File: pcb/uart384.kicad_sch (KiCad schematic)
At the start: 32 parts, among them IC1 ICE40LP384-SG32, J1 USB_A, J2 TC2050, J3 Conn_02x06_Odd_Even, SW1 SW_Push, U1 CP2102-QFN28, U2 AT25DF256-XMHN-T, U3 MIC5365-1.2YC5, Y1 XO32

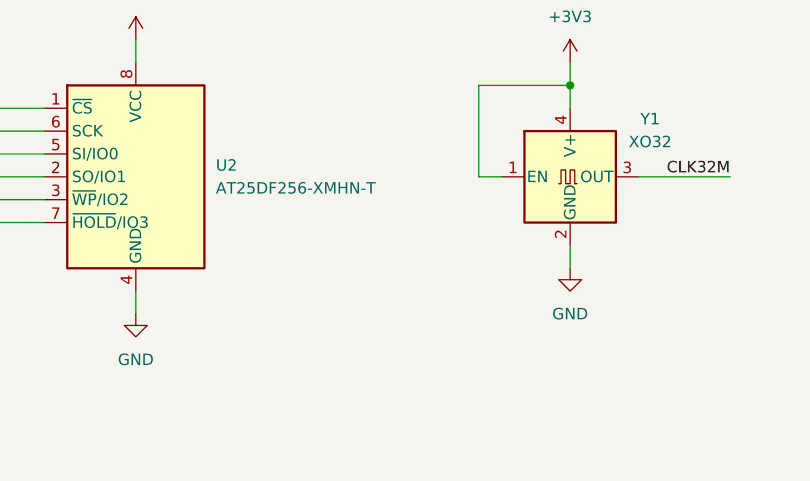
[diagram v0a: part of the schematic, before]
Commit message: PCBv1 Errata: Mismatch between SPI flash footprint and selected part#.
Part now must be SOIC-8 150mil / SOP-8 150mil.
Updated part#s in schematic / PCB.
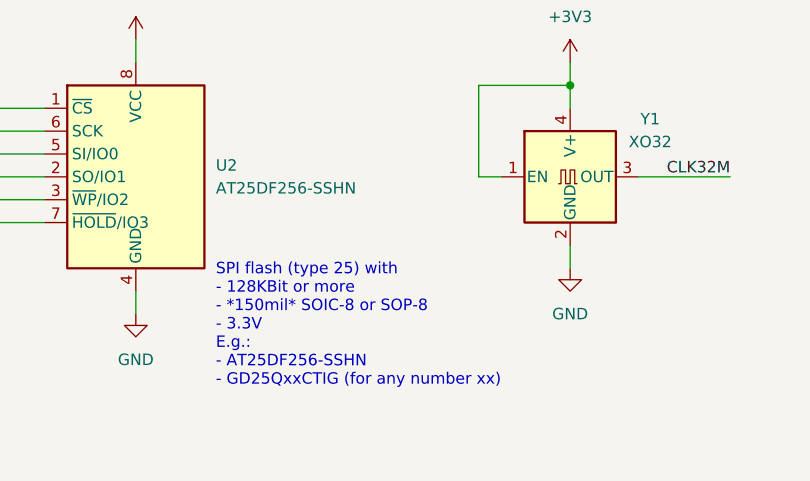
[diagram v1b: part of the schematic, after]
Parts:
- U2: value AT25DF256-XMHN-T -> AT25DF256-SSHN
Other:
- note added: "SPI flash (type 25) with - 128KBit or more - *150mil* SOIC-8 or SOP-8 - 3.3V E.g.: - AT25DF256-SSHN - GD25QxxCTIG (for any number xx)"
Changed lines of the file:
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@@
 	(title_block
 		(title "UART384")
-		(date "2025-08-26")
-		(rev "v1.0")
+		(rev "v1.1~dev")
 		(comment 1 "a USB/UART enabled dev-board for the ice40LP384")
 		(comment 2 "https://github.com/dpiegdon/uart384")
 	)
+	(text "SPI flash (type 25) with\n- 128KBit or more\n- *150mil* SOIC-8 or SOP-8\n- 3.3V\nE.g.:\n- AT25DF256-SSHN\n- GD25QxxCTIG (for any number xx)\n"
+		(exclude_from_sim no)
+		(at 114.3 179.07 0)
+		(effects
+			(font
+				(size 1.27 1.27)
+			)
+			(justify left)
+		)
+	)
 	(text "Close to VCCIO pins"
 		(exclude_from_sim no)
@@
 			)
 		)
-		(property "Value" "AT25DF256-XMHN-T"
+		(property "Value" "AT25DF256-SSHN"
 			(at 114.3 163.8299 0)
 			(effects
@@
 			)
 		)
-		(property "Description" "8-Mbit, 2.5V Minimum SPI Serial Flash Memory with Dual-I/O and Quad-I/O Support, SOIC-8"
+		(property "Description" "Any 3.3V SPI flash with >= 128KBit, SOIC-8 150mil or SOP-8 150mil"
 			(at 105.41 162.56 0)
 			(effects

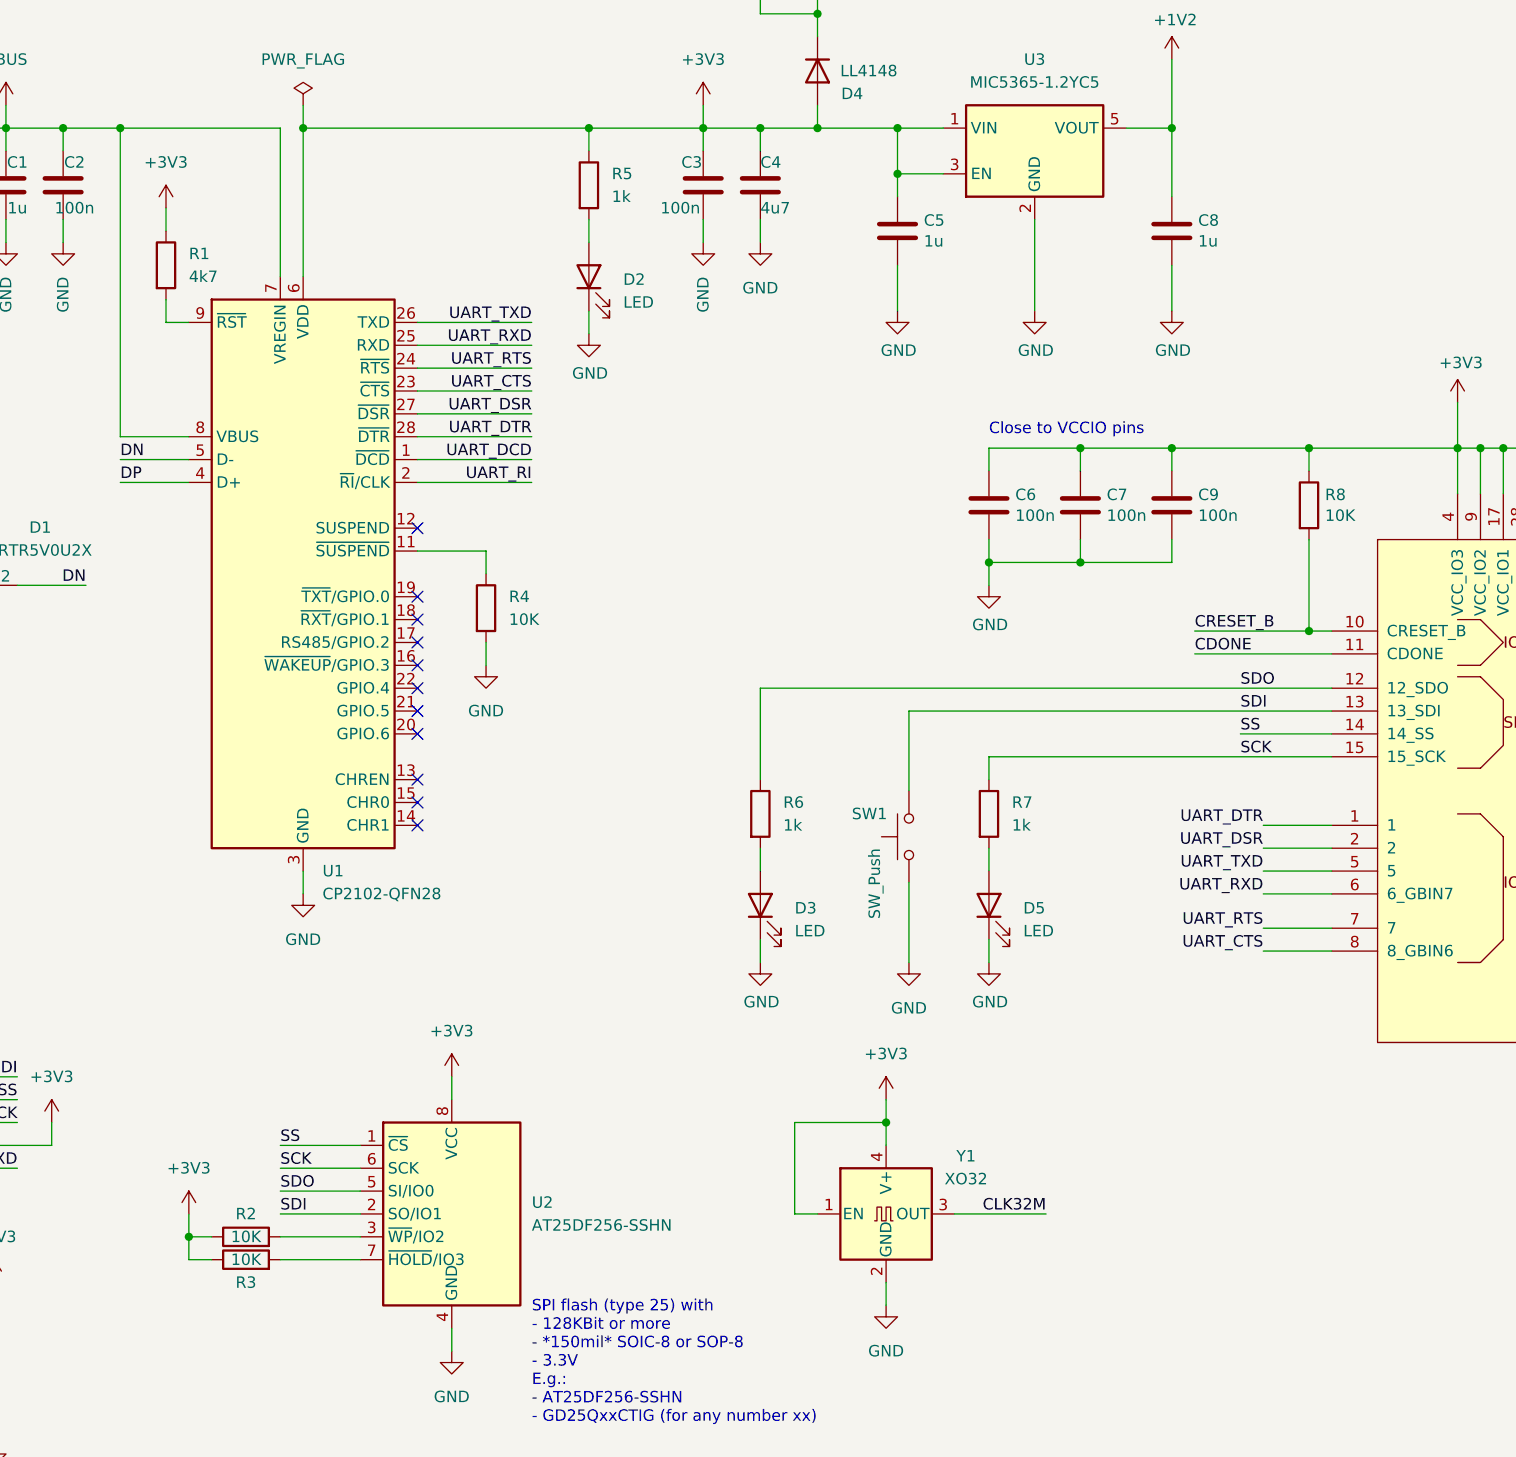
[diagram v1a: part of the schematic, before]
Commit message: PCBv1 Errata: SPI SS pullup missing
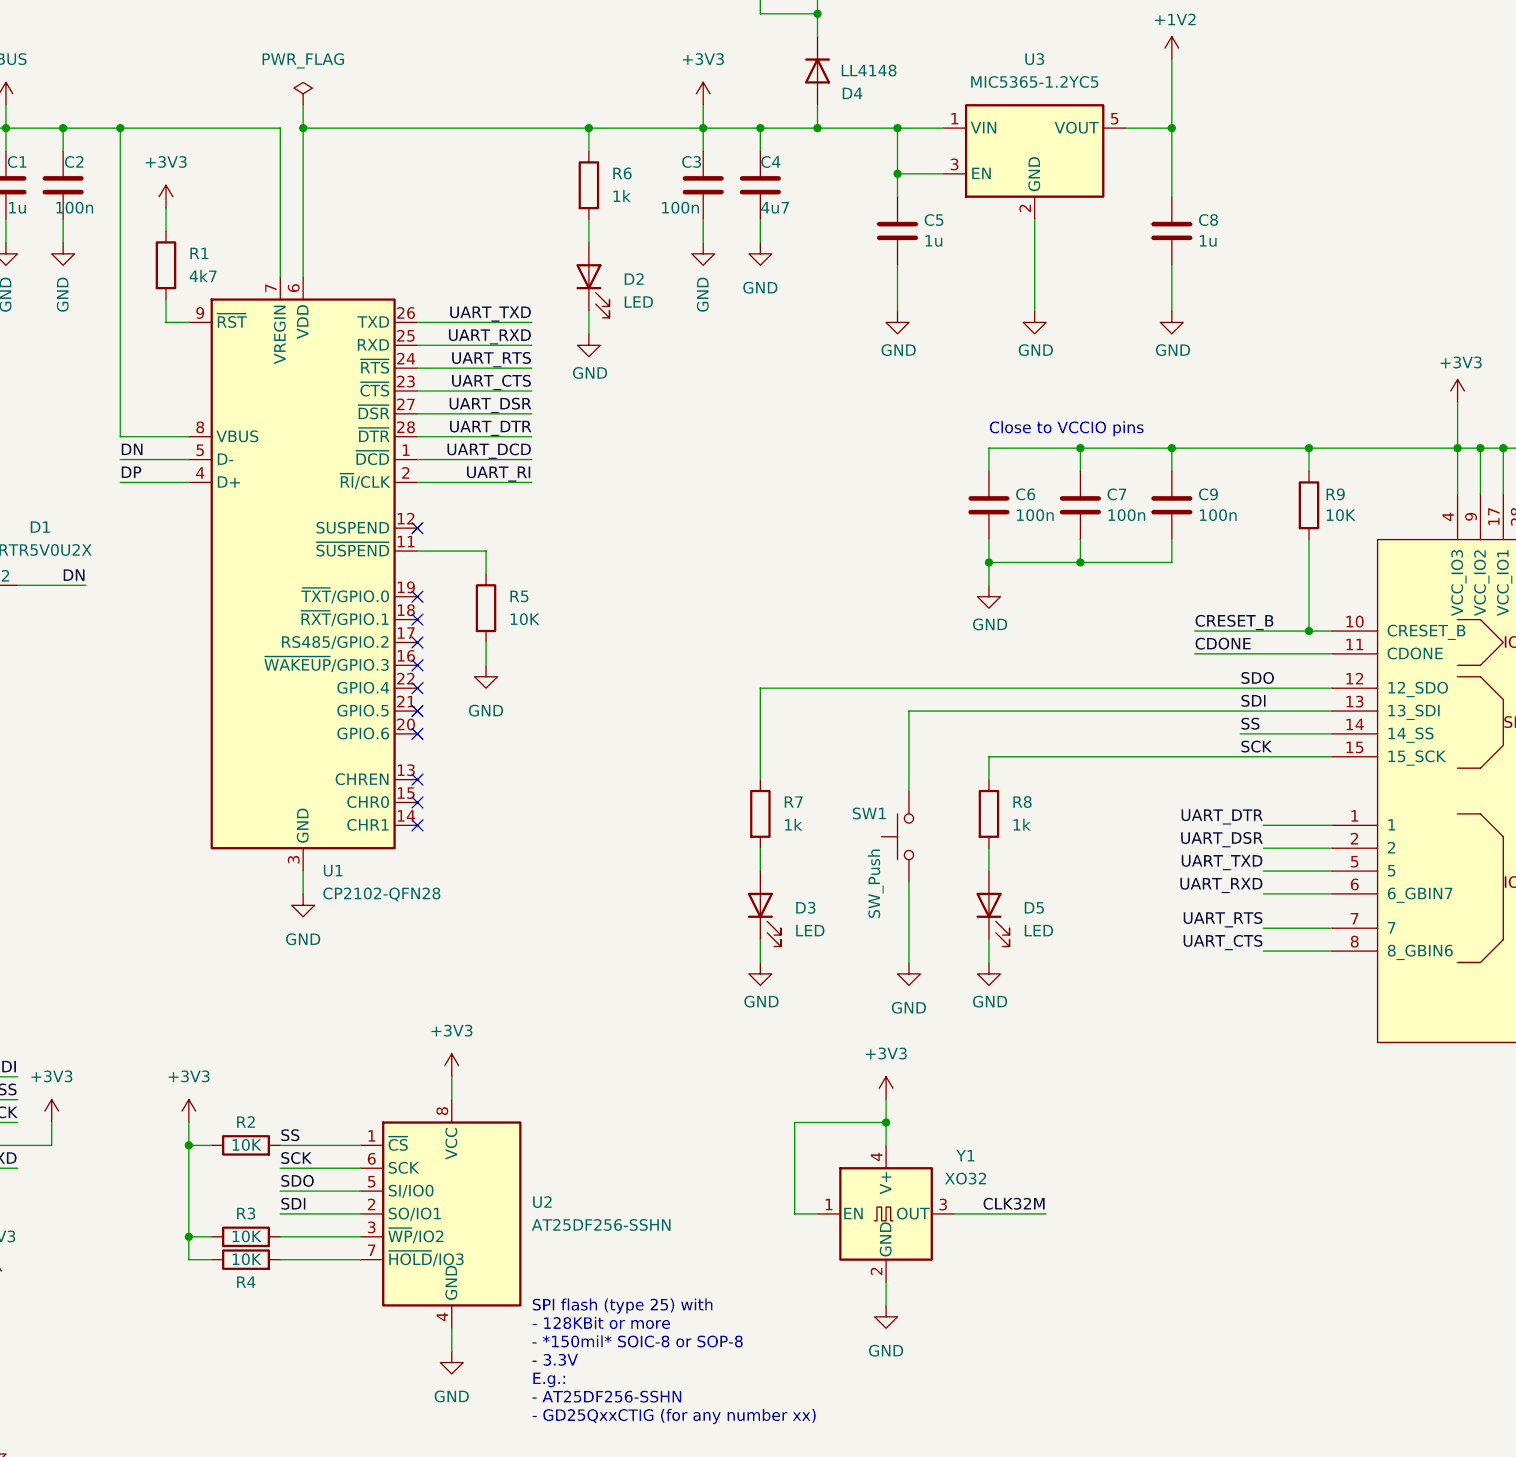
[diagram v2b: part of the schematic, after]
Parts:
- added R2: 10K, Resistor_SMD:R_0603_1608Metric, symbol Device:R
- renumbered R2 to R3, R3 to R4, R4 to R5, R5 to R6, R6 to R7, R7 to R8, R8 to R9
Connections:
- net +3V3: now also R2.1
- net SS: now also R2.2
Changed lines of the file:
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@@
 	)
 	(junction
+		(at 76.2 154.94)
+		(diameter 0)
+		(color 0 0 0 0)
+	)
+	(junction
 		(at 175.26 90.17)
 		(diameter 0)
@@
 	(wire
 		(pts
+			(xy 76.2 154.94) (xy 76.2 165.1)
+		)
+		(stroke
+			(width 0)
+			(type default)
+		)
+	)
+	(wire
+		(pts
 			(xy 139.7 29.21) (xy 146.05 29.21)
 		)
@@
 	(wire
 		(pts
+			(xy 76.2 154.94) (xy 78.74 154.94)
+		)
+		(stroke
+			(width 0)
+			(type default)
+		)
+	)
+	(wire
+		(pts
 			(xy 68.58 41.91) (xy 62.23 41.91)
 		)
@@
 	(wire
 		(pts
-			(xy 76.2 162.56) (xy 76.2 165.1)
+			(xy 76.2 152.4) (xy 76.2 154.94)
 		)
 		(stroke
@@
 		(dnp no)
 		(fields_autoplaced yes)
-		(property "Reference" "R7"
+		(property "Reference" "R8"
 			(at 167.64 116.8399 0)
 			(effects
@@
 			(project ""
 				(path "/951aeac3-6c61-42a5-aa61-f58713889333"
-					(reference "R7")
+					(reference "R8")
 					(unit 1)
 				)
@@
 		(dnp no)
 		(fields_autoplaced yes)
-		(property "Reference" "R4"
+		(property "Reference" "R5"
 			(at 111.76 93.9799 0)
 			(effects
@@
 			(project ""
 				(path "/951aeac3-6c61-42a5-aa61-f58713889333"
-					(reference "R4")
+					(reference "R5")
 					(unit 1)
 				)
@@
 	(symbol
 		(lib_id "power:+3V3")
-		(at 76.2 162.56 0)
+		(at 76.2 152.4 0)
 		(unit 1)
 		(exclude_from_sim no)
@@
 		(fields_autoplaced yes)
 		(property "Reference" "#PWR014"
-			(at 76.2 166.37 0)
+			(at 76.2 156.21 0)
 			(effects
 				(font
@@
 		)
 		(property "Value" "+3V3"
-			(at 76.2 157.48 0)
+			(at 76.2 147.32 0)
 			(effects
 				(font
@@
 		)
 		(property "Footprint" ""
-			(at 76.2 162.56 0)
+			(at 76.2 152.4 0)
 			(effects
 				(font
@@
 		)
 		(property "Datasheet" ""
-			(at 76.2 162.56 0)
+			(at 76.2 152.4 0)
 			(effects
 				(font
@@
 		)
 		(property "Description" "Power symbol creates a global label with name \"+3V3\""
-			(at 76.2 162.56 0)
+			(at 76.2 152.4 0)
 			(effects
 				(font
@@
 		(on_board yes)
 		(dnp no)
-		(property "Reference" "R3"
+		(property "Reference" "R4"
 			(at 82.55 170.18 90)
 			(effects
@@
 			(project ""
 				(path "/951aeac3-6c61-42a5-aa61-f58713889333"
-					(reference "R3")
+					(reference "R4")
 					(unit 1)
 				)
@@
 		(on_board yes)
 		(dnp no)
-		(property "Reference" "R2"
+		(property "Reference" "R3"
 			(at 82.55 162.56 90)
 			(effects
@@
 			(project ""
 				(path "/951aeac3-6c61-42a5-aa61-f58713889333"
-					(reference "R2")
+					(reference "R3")
 					(unit 1)
 				)
@@
 		(on_board yes)
 		(dnp no)
-		(property "Reference" "R8"
+		(property "Reference" "R9"
 			(at 202.438 82.6516 0)
 			(effects
@@
 			(project "uart384"
 				(path "/951aeac3-6c61-42a5-aa61-f58713889333"
-					(reference "R8")
+					(reference "R9")
 					(unit 1)
 				)
@@
 		(dnp no)
 		(fields_autoplaced yes)
-		(property "Reference" "R6"
+		(property "Reference" "R7"
 			(at 142.24 116.8399 0)
 			(effects
@@
 			(project "uart384"
 				(path "/951aeac3-6c61-42a5-aa61-f58713889333"
-					(reference "R6")
+					(reference "R7")
 					(unit 1)
 				)
@@
 	)
 	(symbol
+		(lib_id "Device:R")
+		(at 82.55 154.94 90)
+		(unit 1)
+		(exclude_from_sim no)
+		(in_bom yes)
+		(on_board yes)
+		(dnp no)
+		(property "Reference" "R2"
+			(at 82.55 152.4 90)
+			(effects
+				(font
+					(size 1.27 1.27)
+				)
+			)
+		)
+		(property "Value" "10K"
+			(at 82.55 154.94 90)
+			(effects
+				(font
+					(size 1.27 1.27)
+				)
+			)
+		)
+		(property "Footprint" "Resistor_SMD:R_0603_1608Metric"
+			(at 82.55 156.718 90)
+			(effects
+				(font
+					(size 1.27 1.27)
+				)
+				(hide yes)
+			)
+		)
+		(property "Datasheet" "~"
+			(at 82.55 154.94 0)
+			(effects
+				(font
+					(size 1.27 1.27)
+				)
+				(hide yes)
+			)
+		)
+		(property "Description" "Resistor"
+			(at 82.55 154.94 0)
+			(effects
+				(font
+					(size 1.27 1.27)
+				)
+				(hide yes)
+			)
+		)
+		(pin "2"
+		)
+		(pin "1"
+		)
+		(instances
+			(project "uart384"
+				(path "/951aeac3-6c61-42a5-aa61-f58713889333"
+					(reference "R2")
+					(unit 1)
+				)
+			)
+		)
+	)
+	(symbol
 		(lib_id "Device:C")
 		(at 139.7 48.26 0)
@@
 		(dnp no)
 		(fields_autoplaced yes)
-		(property "Reference" "R5"
+		(property "Reference" "R6"
 			(at 123.19 46.9899 0)
 			(effects
@@
 			(project "uart384"
 				(path "/951aeac3-6c61-42a5-aa61-f58713889333"
-					(reference "R5")
+					(reference "R6")
 					(unit 1)
 				)

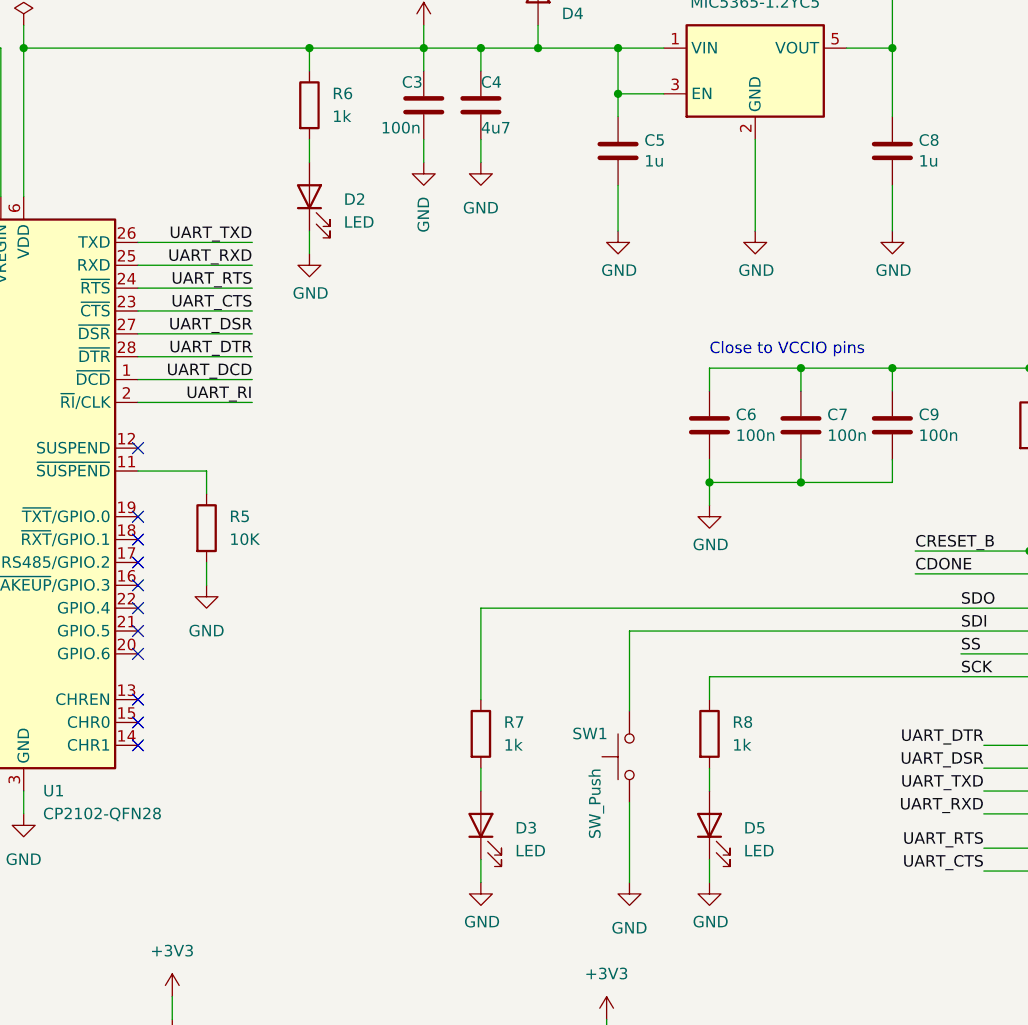
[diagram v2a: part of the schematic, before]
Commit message: name LEDs with used colors. use LEDs for more things.
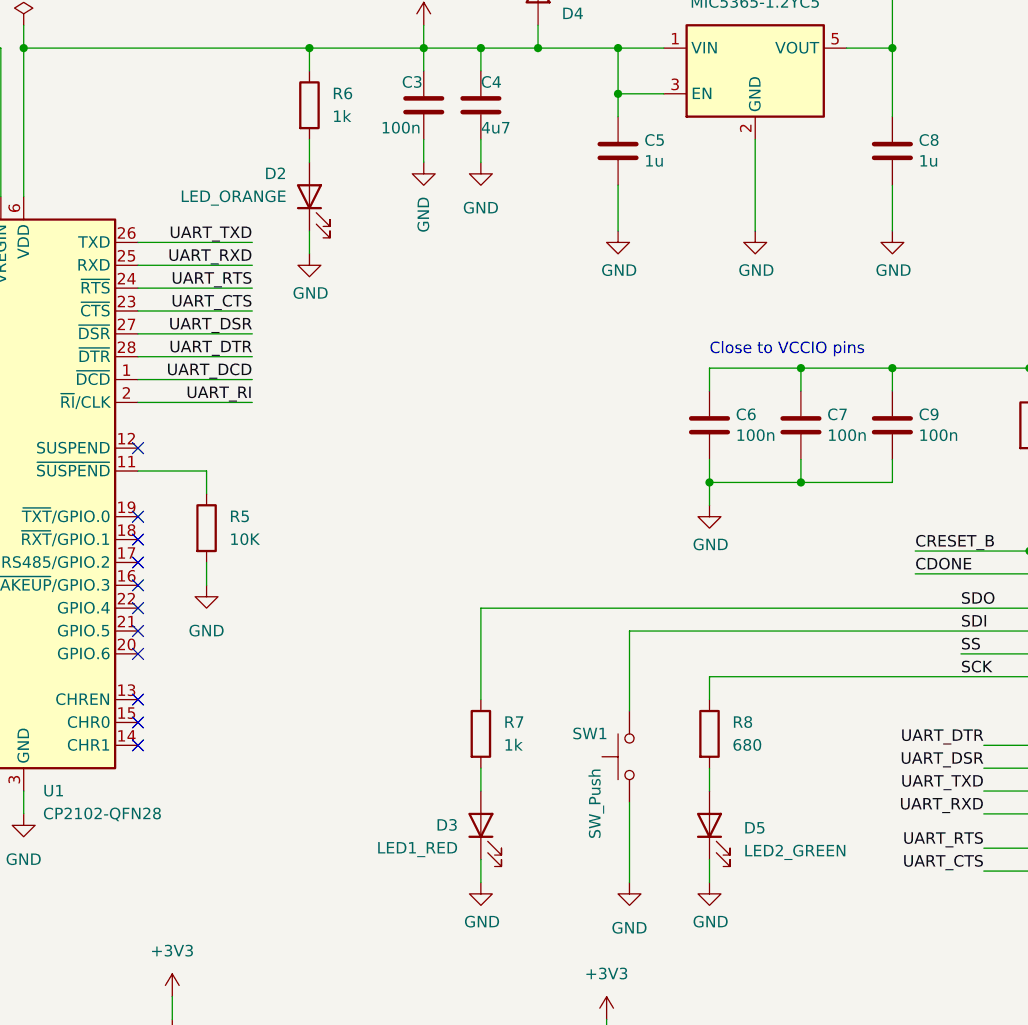
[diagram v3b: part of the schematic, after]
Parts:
- D2: value LED -> LED_ORANGE
- D3: value LED -> LED1_RED
- D5: value LED -> LED2_GREEN
- R8: value 1k -> 680
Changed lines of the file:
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@@
 			)
 		)
-		(property "Value" "1k"
+		(property "Value" "680"
 			(at 167.64 119.3799 0)
 			(effects
@@
 		(on_board yes)
 		(dnp no)
-		(fields_autoplaced yes)
 		(property "Reference" "D2"
-			(at 124.46 58.7374 90)
-			(effects
-				(font
-					(size 1.27 1.27)
-				)
-				(justify right)
-			)
-		)
-		(property "Value" "LED"
-			(at 124.46 61.2774 90)
-			(effects
-				(font
-					(size 1.27 1.27)
-				)
-				(justify right)
+			(at 118.11 55.88 90)
+			(effects
+				(font
+					(size 1.27 1.27)
+				)
+				(justify left)
+			)
+		)
+		(property "Value" "LED_ORANGE"
+			(at 118.11 58.42 90)
+			(effects
+				(font
+					(size 1.27 1.27)
+				)
+				(justify left)
 			)
 		)
@@
 			)
 		)
-		(property "Value" "LED"
+		(property "Value" "LED2_GREEN"
 			(at 168.91 131.1274 90)
 			(effects
@@
 		(on_board yes)
 		(dnp no)
-		(fields_autoplaced yes)
 		(property "Reference" "D3"
-			(at 143.51 128.5874 90)
-			(effects
-				(font
-					(size 1.27 1.27)
-				)
-				(justify right)
-			)
-		)
-		(property "Value" "LED"
-			(at 143.51 131.1274 90)
-			(effects
-				(font
-					(size 1.27 1.27)
-				)
-				(justify right)
-			)
-		)
+			(at 137.16 128.27 90)
+			(effects
+				(font
+					(size 1.27 1.27)
+				)
+				(justify left)
+			)
+		)
+		(property "Value" "LED1_RED"
+			(at 137.16 130.81 90)
+			(effects
+				(font
+					(size 1.27 1.27)
+				)
+				(justify left)
+			)
+		)
